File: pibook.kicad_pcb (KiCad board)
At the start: 2 copper layers, 100 x 85 mm, 148 parts, among them IC1 ATTINY48-A, J1 ComputeModule, J2 TRS_JACK_3PIN, P1 CONN_01X40, P2 USB_OTG, P3 CONN_01X02, P4 CONN_02X05, P5 USB_A, P6 CONN_02X06, Q1 Si2323DS, Q2 Si2323DS, Q3 BSS138P, Q4 Si2323DS, SW1 SW_SMT_4PIN_6X3, SW10 SW_SMT_4PIN_6X3, SW11 SW_SMT_4PIN_6X3, SW12 SW_SMT_4PIN_6X3, SW13 SW_SMT_4PIN_6X3, SW14 SW_SMT_4PIN_6X3, SW15 SW_SMT_4PIN_6X3, SW16 SW_SMT_4PIN_6X3, SW17 SW_SMT_4PIN_6X3, SW18 SW_SMT_4PIN_6X3, SW19 SW_SMT_4PIN_6X3, SW2 SW_SMT_4PIN_6X3, SW20 SW_SMT_4PIN_6X3, SW21 SW_SMT_4PIN_6X3, SW22 SW_SMT_4PIN_6X3, SW23 SW_SMT_4PIN_6X3, SW24 SW_SMT_4PIN_6X3, SW25 SW_SMT_4PIN_6X3, SW26 SW_SMT_4PIN_6X3, SW27 SW_SMT_4PIN_6X3, SW28 SW_SMT_4PIN_6X3, SW29 SW_SMT_4PIN_6X3, SW3 SW_SMT_4PIN_6X3, SW30 SW_SMT_4PIN_6X3, SW31 SW_SMT_4PIN_6X3, SW32 SW_SMT_4PIN_6X3, SW33 SW_SMT_4PIN_6X3, SW34 SW_SMT_4PIN_6X3, SW35 SW_SMT_4PIN_6X3, SW36 SW_SMT_4PIN_6X3, SW37 SW_SMT_4PIN_6X3, SW38 SW_SMT_4PIN_6X3, SW39 SW_SMT_4PIN_6X3, SW4 SW_SMT_4PIN_6X3, SW40 SW_SMT_4PIN_6X3, SW41 SW_SMT_4PIN_6X3, SW42 SW_SMT_4PIN_6X3, SW43 SW_SMT_4PIN_6X3, SW44 SW_SMT_4PIN_6X3, SW45 SW_SMT_4PIN_6X3, SW46 SW_SMT_4PIN_6X3, SW47 SW_SMT_4PIN_6X3, SW48 SW_SMT_4PIN_6X3, SW49 SW_SMT_4PIN_6X3, SW5 SW_SMT_4PIN_6X3, SW50 SW_SMT_4PIN_6X3, SW51 SW_SMT_4PIN_6X3, SW52 SW_SMT_4PIN_6X3, SW53 SW_SMT_4PIN_6X3, SW54 SW_SMT_4PIN_6X3, SW55 SW_SMT_4PIN_6X3, SW56 SW_SMT_4PIN_6X3, SW57 SW_SMT_4PIN_6X3, SW58 SW_SMT_4PIN_6X3, SW59 SW_SMT_4PIN_6X3, SW6 SW_SMT_4PIN_6X3, SW60 SW_SMT_4PIN_6X3, SW61 SW_SMT_4PIN_6X3, SW62 SW_SMT_4PIN_6X3, SW63 SW_SMT_4PIN_6X3, SW64 SW_SMT_4PIN_6X3, SW65 SW_SMT_4PIN_6X3, SW66 SW_SMT_4PIN_6X3, SW67 SW_SMT_4PIN_6X3, SW68 SW_SMT_4PIN_6X3, SW69 SW_SMT_4PIN_6X3, SW7 SW_SMT_4PIN_6X3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

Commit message: Components all on PCB
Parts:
- added R18: 100k, Resistors_SMD:R_0603, F.Cu at (137.0, 142.0)
- added R19: 100k, Resistors_SMD:R_0603, F.Cu at (168.0, 128.0)
- added R20: 100k, Resistors_SMD:R_0603, F.Cu at (168.0, 108.0)
- added R21: 100k, Resistors_SMD:R_0603, F.Cu at (168.0, 130.0)
- added R22: 100k, Resistors_SMD:R_0603, F.Cu at (168.0, 110.0)
- added SW91: SPST, ComputeModule:SPDT_SLIDE_SWITCH, F.Cu at (162.0, 64.0)
- added W15: TEST_1P, Measurement_Points:Measurement_Point_Round-SMD-Pad_Small, F.Cu at (138.0, 145.0)
- C2: moved to B.Cu
- R1: value 470k -> 100k
- SW1, SW10, SW11, SW12, SW13, SW14, SW15, SW16, SW17, SW18, SW19, SW2, SW20, SW21, SW22, SW23, SW24, SW25, SW26, SW27, SW28, SW29, SW3, SW30, SW31, SW32, SW33, SW34, SW35, SW36, SW37, SW38, SW39, SW4, SW40, SW41, SW42, SW43, SW44, SW45, SW46, SW47, SW48, SW49, SW5, SW50, SW51, SW52, SW53, SW54, SW55, SW56, SW57, SW58, SW59, SW6, SW60, SW61, SW62, SW63, SW64, SW65, SW66, SW67, SW68, SW69, SW7, SW70, SW71, SW72, SW8, SW9: footprint ComputeModule:TACT_SWITCH_SMD_6X3MM -> ComputeModule:TACT_SWITCH_SMD_6X3MM_NOTEXT
- moved W5 146.2 mm to (140.0, 145.0)
- moved R2 141.0 mm to (135.0, 142.0), turned to 270 degrees
- moved SW1 120.5 mm to (158.0, 86.0)
- moved SW10 120.5 mm to (152.0, 116.0)
- moved SW11 120.5 mm to (152.0, 126.0)
- moved SW12 120.5 mm to (152.0, 136.0)
- moved SW13 120.5 mm to (146.0, 86.0)
- moved SW14 120.5 mm to (146.0, 96.0)
- moved SW15 120.5 mm to (146.0, 106.0)
- moved SW16 120.5 mm to (146.0, 116.0)
- moved SW17 120.5 mm to (146.0, 126.0)
- moved SW18 120.5 mm to (146.0, 136.0)
- moved SW19 120.5 mm to (140.0, 86.0)
- moved SW2 120.5 mm to (158.0, 96.0)
- moved SW20 120.5 mm to (140.0, 96.0)
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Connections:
- IC1 pad 20: (no net) -> /LCD_DISP_ON
- J1 pad 28: (no net) -> Net-(J1-Pad28)
- J1 pad 30: (no net) -> Net-(J1-Pad30)
- J1 pad 82: (no net) -> Net-(J1-Pad82)
- J1 pad 84: (no net) -> Net-(J1-Pad84)
- P1 pad 31: (no net) -> /LCD_DISP_ON
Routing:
- net /LCD_DEN: track 0.00 -> 101.5 mm
- net /LCD_CLK: track 0.00 -> 92.4 mm
- net GND: track 0.60 -> 0.00 mm
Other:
- outline, holes or cut-outs redrawn

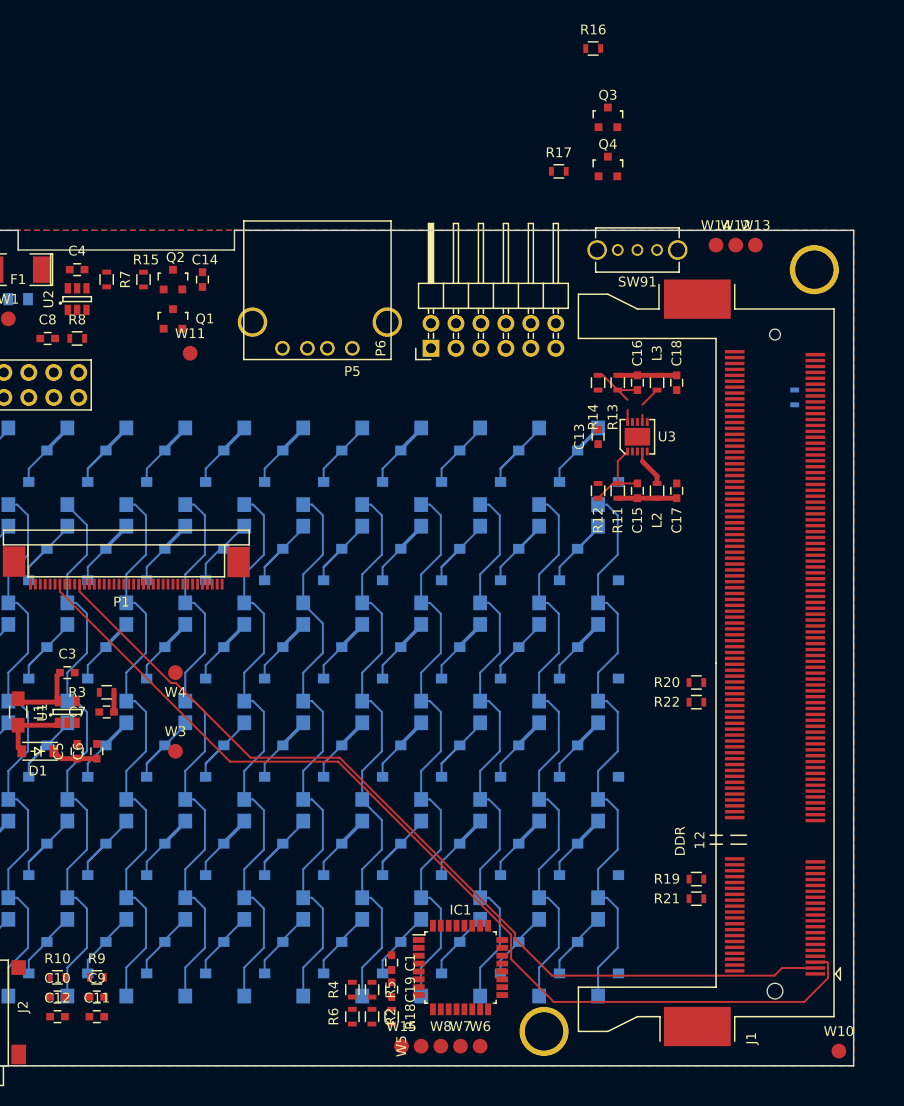
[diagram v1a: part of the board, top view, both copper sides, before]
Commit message: Routed DPI bus
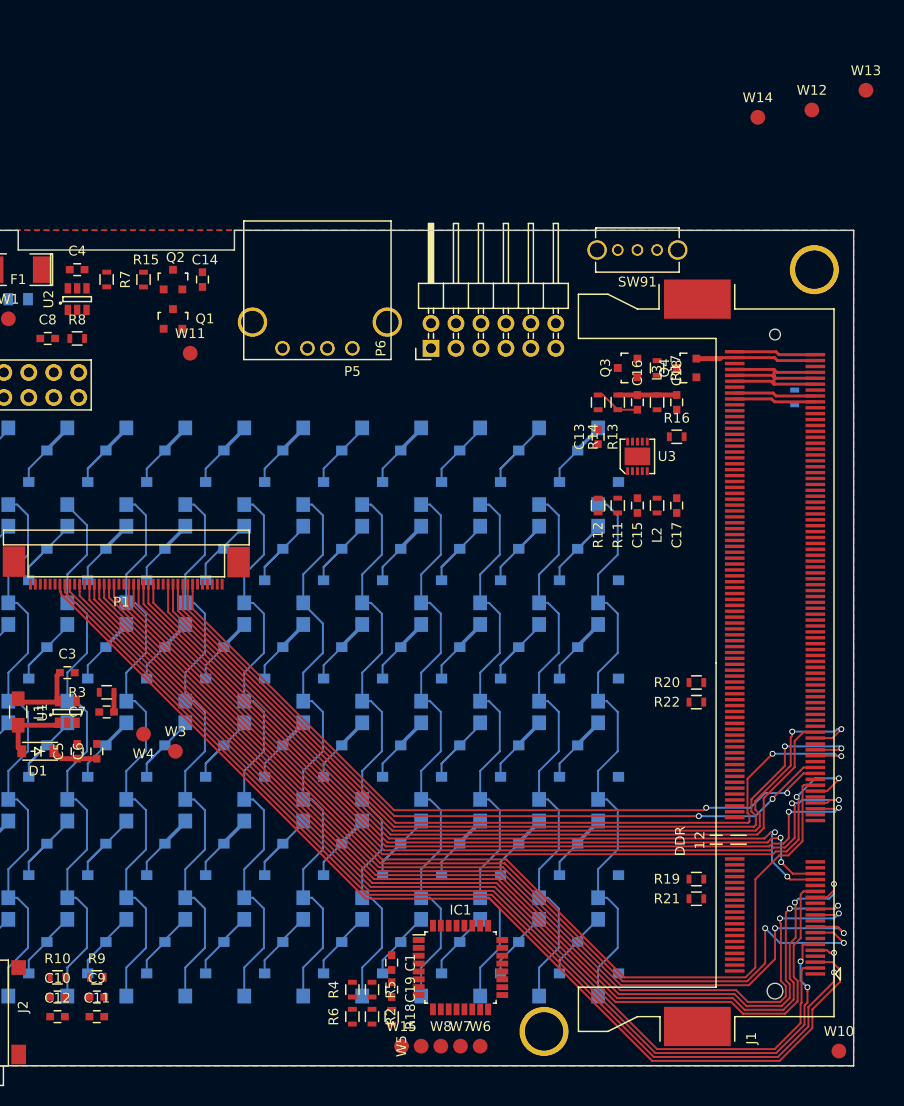
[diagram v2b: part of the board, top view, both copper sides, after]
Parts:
- moved R16 40.4 mm to (166.0, 83.0)
- moved Q3 25.6 mm to (161.0, 76.0), turned to 90 degrees
- moved R17 22.4 mm to (164.0, 76.0), turned to 270 degrees
- moved Q4 22.0 mm to (167.0, 76.0), turned to 90 degrees
- moved W13 19.4 mm to (185.2, 47.8)
- moved W12 15.8 mm to (179.8, 49.8)
- moved W14 13.7 mm to (174.2, 50.5)
- moved W4 7.04 mm to (111.8, 113.2)
- moved C16 2.00 mm to (162.0, 79.5)
- moved C18 2.00 mm to (166.0, 79.5)
- moved L3 2.00 mm to (164.0, 79.5)
- moved R13 2.00 mm to (160.0, 79.5)
- moved R14 2.00 mm to (158.0, 79.5)
- moved U3 2.00 mm to (162.0, 85.0)
- moved C15 1.50 mm to (162.0, 90.0)
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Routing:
- net /LCD_B_6: track 0.00 -> 108.9 mm, vias 0 -> 2
- net /LCD_VSYNC: track 0.00 -> 107.9 mm, vias 0 -> 2
- net /LCD_B_5: track 0.00 -> 106.1 mm, vias 0 -> 2
- net /LCD_HSYNC: track 0.00 -> 106.1 mm, vias 0 -> 2
- net /LCD_B_4: track 0.00 -> 104.9 mm, vias 0 -> 2
- net /LCD_B_7: track 0.00 -> 104.6 mm
- net /LCD_G_7: track 0.00 -> 104.4 mm
- net /LCD_B_3: track 0.00 -> 100.1 mm, vias 0 -> 2
- net /LCD_B_2: track 0.00 -> 100.0 mm, vias 0 -> 2
- net /LCD_G_6: track 0.00 -> 93.4 mm, vias 0 -> 2
- net /LCD_R_6: track 0.00 -> 91.4 mm, vias 0 -> 2
- net /LCD_G_5: track 0.00 -> 90.8 mm, vias 0 -> 2
- net /LCD_R_5: track 0.00 -> 88.8 mm, vias 0 -> 2
- net /LCD_G_4: track 0.00 -> 88.4 mm, vias 0 -> 2
- net /LCD_R_4: track 0.00 -> 87.1 mm, vias 0 -> 2
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
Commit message: USB + some power routing
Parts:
- C2: moved to F.Cu
- R16: moved to B.Cu
- moved R16 14.8 mm to (163.0, 68.5)
- moved C18 13.2 mm to (158.0, 90.0), turned to 90 degrees
- moved R14 13.2 mm to (166.0, 90.0)
- moved C17 12.8 mm to (158.0, 80.0), turned to 270 degrees
- moved R12 12.8 mm to (166.0, 80.0)
- moved L3 11.2 mm to (160.0, 90.0), turned to 270 degrees
- moved R13 11.2 mm to (164.0, 90.0), turned to 90 degrees
- moved L2 10.8 mm to (160.0, 80.0), turned to 90 degrees
- moved R11 10.8 mm to (164.0, 80.0), turned to 270 degrees
- moved C16 10.5 mm to (162.0, 90.0), turned to 90 degrees
- moved C15 10.0 mm to (162.0, 80.0), turned to 270 degrees
- moved W1 4.47 mm to (102.0, 69.0)
- moved P6 2.46 mm to (140.9, 71.5)
- moved C13 2.00 mm to (158.0, 85.0), turned to 270 degrees
- moved D2 1.50 mm to (87.5, 82.0), turned to 180 degrees
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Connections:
- J1 pad 165: /USB_DP -> /USB_D+
- J1 pad 167: /USB_DM -> /USB_D-
- P5 pad 2: /USB_DM -> /USB_D+
- P5 pad 3: /USB_DP -> /USB_D-
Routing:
- net +BATT: track 7.22 -> 133.9 mm
- net /USB_D+: track 0.00 -> 93.0 mm
- net /USB_D-: track 0.00 -> 88.6 mm
- net /PWR_ENABLE: track 0.00 -> 27.3 mm, vias 0 -> 2
- net +VUSB_OUT: track 0.00 -> 26.2 mm
- net +VUSB_IN: track 0.00 -> 20.4 mm
- net +1V8: track 22.6 -> 42.1 mm
- net +3V3: track 26.8 -> 41.9 mm
- net Net-(F1-Pad2): track 0.00 -> 8.53 mm
- net Net-(Q3-Pad3): track 0.00 -> 8.39 mm
- net Net-(C15-Pad2): track 0.00 -> 7.16 mm
- net Net-(L3-Pad1): track 0.00 -> 3.37 mm
- net Net-(L2-Pad1): track 0.00 -> 3.37 mm
- net Net-(Q2-Pad3): track 0.00 -> 3.26 mm
- net Net-(C16-Pad2): track 4.62 -> 7.01 mm

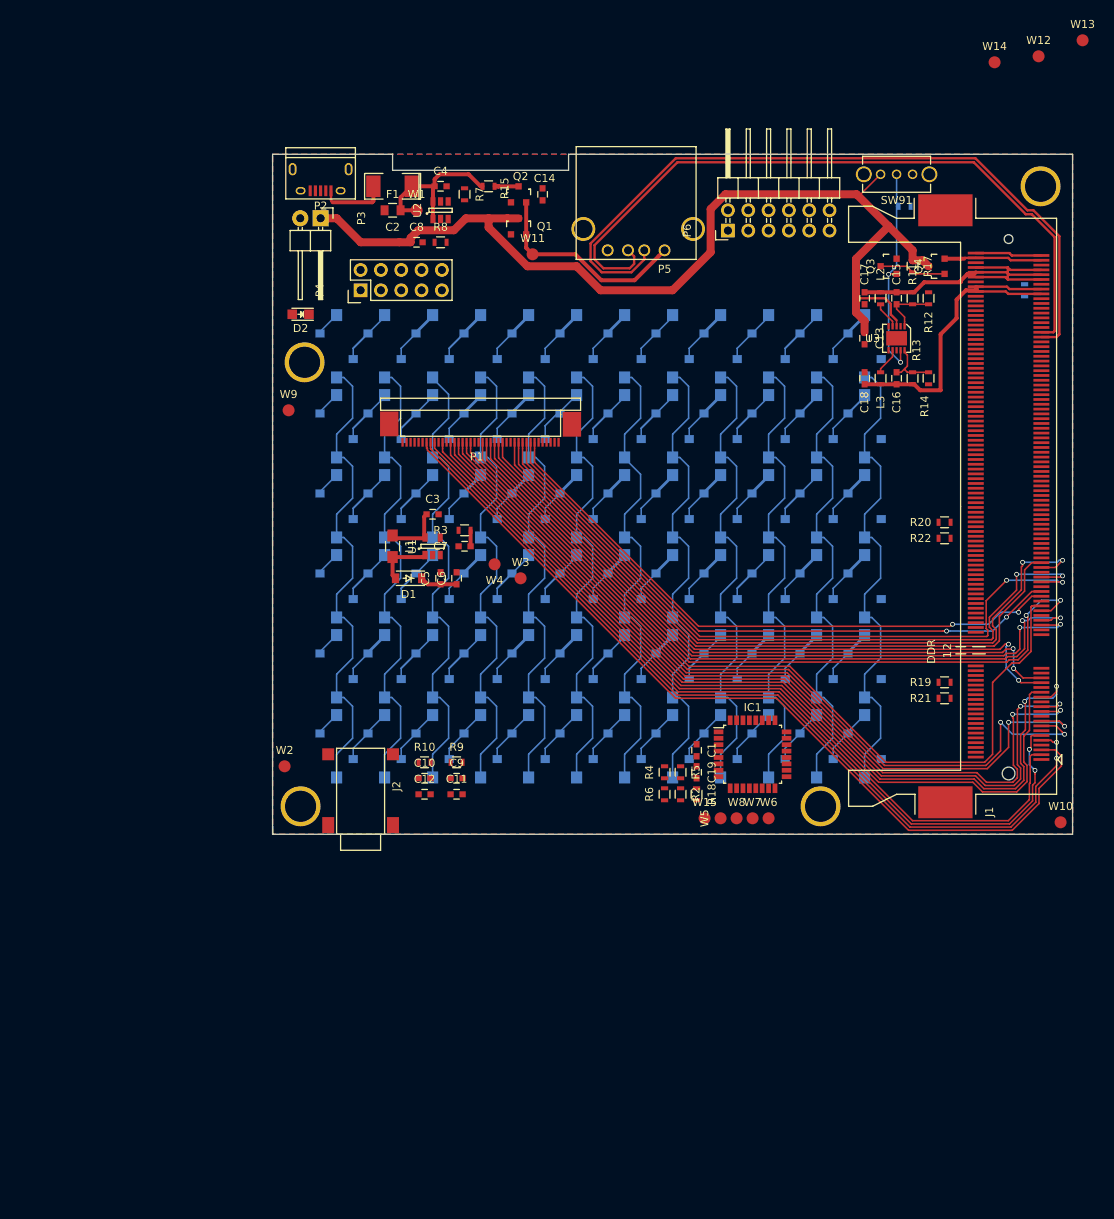
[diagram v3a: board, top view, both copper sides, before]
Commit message: New mechanical board layout
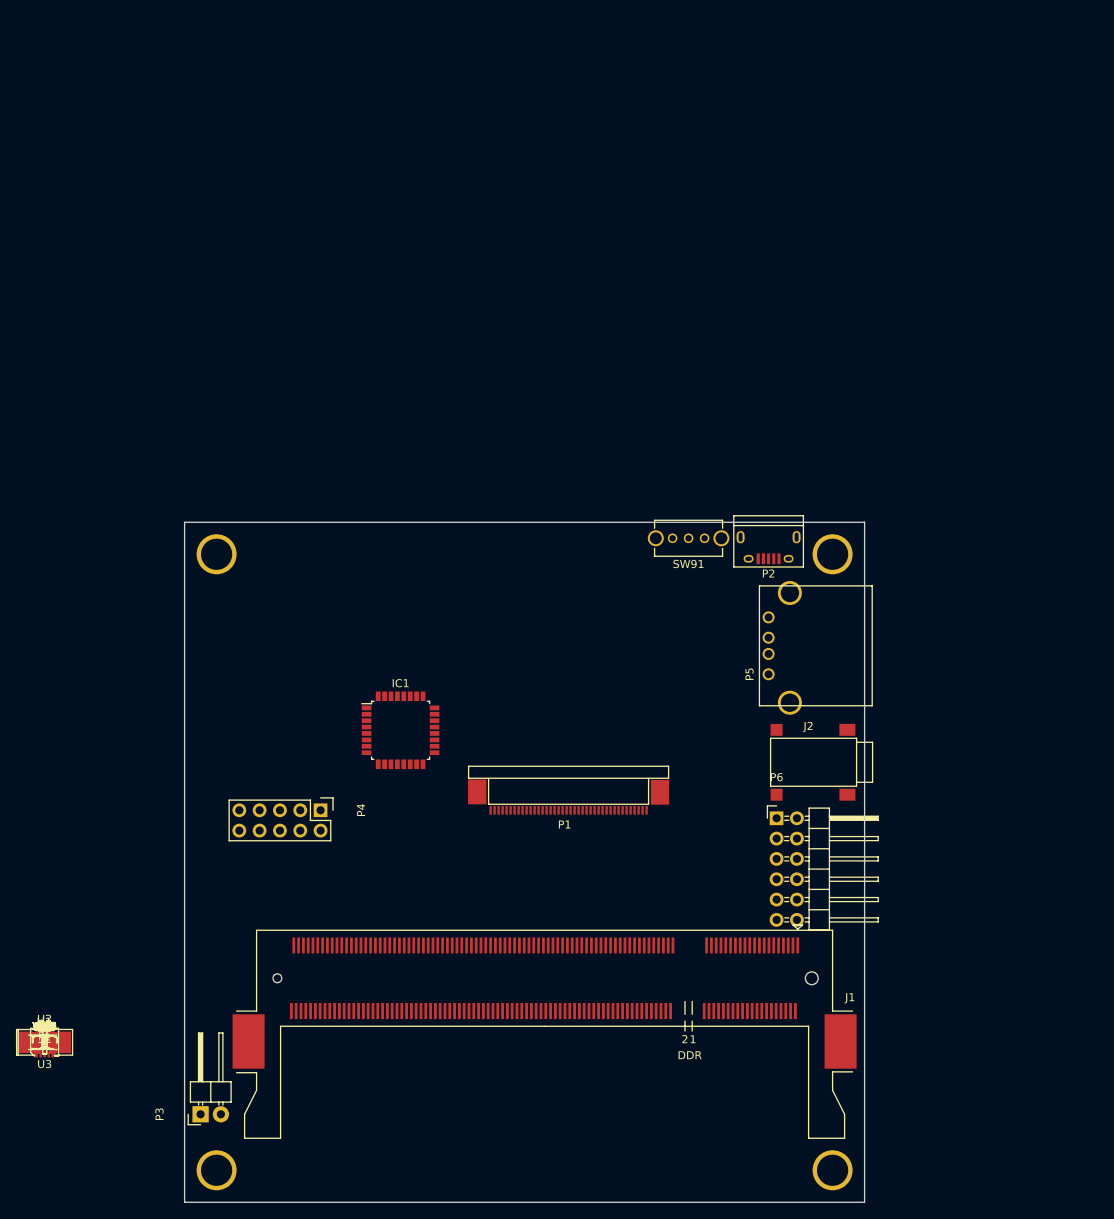
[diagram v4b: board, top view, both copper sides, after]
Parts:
- removed SW1, SW10, SW11, SW12, SW13, SW14, SW15, SW16, SW17, SW18, SW19, SW2, SW20, SW21, SW22, SW23, SW24, SW25, SW26, SW27, SW28, SW29, SW3, SW30, SW31, SW32, SW33, SW34, SW35, SW36, SW37, SW38, SW39, SW4, SW40, SW41, SW42, SW43, SW44, SW45, SW46, SW47, SW48, SW49, SW5, SW50, SW51, SW52, SW53, SW54, SW55, SW56, SW57, SW58, SW59, SW6, SW60, SW61, SW62, SW63, SW64, SW65, SW66, SW67, SW68, SW69, SW7, SW70, SW71, SW72, SW8, SW9: SW_SMT_4PIN_6X3, ComputeModule:TACT_SWITCH_SMD_6X3MM_NOTEXT
- R1, R16: moved to F.Cu
- moved W13 180.3 mm to (55.5, 173.0)
- moved W12 175.0 mm to (55.5, 173.0)
- moved W14 170.6 mm to (55.5, 173.0)
- moved R1 154.4 mm to (55.5, 173.0), turned to 0 degrees
- moved R16 149.9 mm to (55.5, 173.0)
- moved Q4 147.8 mm to (55.5, 173.0), turned to 0 degrees
- moved R17 145.5 mm to (55.5, 173.0), turned to 0 degrees
- moved R12 144.4 mm to (55.5, 173.0), turned to 0 degrees
- moved Q3 143.3 mm to (55.5, 173.0), turned to 0 degrees
- moved R11 142.9 mm to (55.5, 173.0), turned to 0 degrees
- moved C15 141.4 mm to (55.5, 173.0), turned to 0 degrees
- moved L2 139.9 mm to (55.5, 173.0), turned to 0 degrees
- moved C17 138.4 mm to (55.5, 173.0), turned to 0 degrees
- moved R14 138.2 mm to (55.5, 173.0), turned to 0 degrees
- moved U3 138.2 mm to (55.5, 173.0), turned to 0 degrees
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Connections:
- IC1 pad 1: /KEY_C3 -> (no net)
- IC1 pad 10: /KEY_C6 -> (no net)
- IC1 pad 11: /KEY_C7 -> (no net)
- IC1 pad 12: /KEY_R1 -> (no net)
- IC1 pad 2: /KEY_C4 -> (no net)
- IC1 pad 23: /KEY_C8 -> (no net)
- IC1 pad 24: /KEY_C9 -> (no net)
- IC1 pad 25: /KEY_C10 -> (no net)
- IC1 pad 26: /KEY_C11 -> (no net)
- IC1 pad 27: /KEY_R0 -> (no net)
- IC1 pad 3: /KEY_R4 -> (no net)
- IC1 pad 30: /KEY_C0 -> (no net)
- IC1 pad 31: /KEY_C1 -> (no net)
- IC1 pad 32: /KEY_C2 -> (no net)
- IC1 pad 6: /KEY_R5 -> (no net)
- IC1 pad 7: /KEY_R2 -> (no net)
- IC1 pad 8: /KEY_R3 -> (no net)
- IC1 pad 9: /KEY_C5 -> (no net)
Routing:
- net +BATT: track 133.9 -> 0.00 mm
- net /LCD_B_6: track 108.9 -> 0.00 mm, vias 2 -> 0
- net /LCD_DEN: track 108.5 -> 0.00 mm
- net /LCD_VSYNC: track 107.9 -> 0.00 mm, vias 2 -> 0
- net /LCD_B_5: track 106.1 -> 0.00 mm, vias 2 -> 0
- net /LCD_HSYNC: track 106.1 -> 0.00 mm, vias 2 -> 0
- net /LCD_B_4: track 104.9 -> 0.00 mm, vias 2 -> 0
- net /LCD_B_7: track 104.6 -> 0.00 mm
- net /LCD_G_7: track 104.4 -> 0.00 mm
- net /LCD_CLK: track 101.7 -> 0.00 mm
- net /LCD_B_3: track 100.1 -> 0.00 mm, vias 2 -> 0
- net /LCD_B_2: track 100.0 -> 0.00 mm, vias 2 -> 0
- net /LCD_G_6: track 93.4 -> 0.00 mm, vias 2 -> 0
- net /USB_D+: track 93.0 -> 0.00 mm
- net /LCD_R_6: track 91.4 -> 0.00 mm, vias 2 -> 0
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- removed copper zone on B.Cu, net GND
- removed copper zone on F.Cu, net GND
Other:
- board size 100 x 85 mm -> 85 x 85 mm
- net class Default: trace_width 0.2 -> 0.25
- net class Power_1A removed
- net class Power_500mA removed
- rule pad_to_mask_clearance: 0.2 -> 0
- board text added: "Screen + FFC"
